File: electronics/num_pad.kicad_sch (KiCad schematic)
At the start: 22 parts, among them J17 Conn_01x04, J18 Conn_01x04, J19 Conn_01x04, J20 Conn_01x04, SW69 SW_SPST, SW70 SW_SPST, SW71 SW_SPST, SW72 SW_SPST, SW73 SW_SPST, SW74 SW_SPST, SW75 SW_SPST, SW76 SW_SPST, SW77 SW_SPST, SW78 SW_SPST, SW79 SW_SPST, SW80 SW_SPST, SW81 SW_SPST, SW82 SW_SPST, SW83 SW_SPST, SW84 SW_SPST, SW85 SW_SPST, U5 PCA9675PW

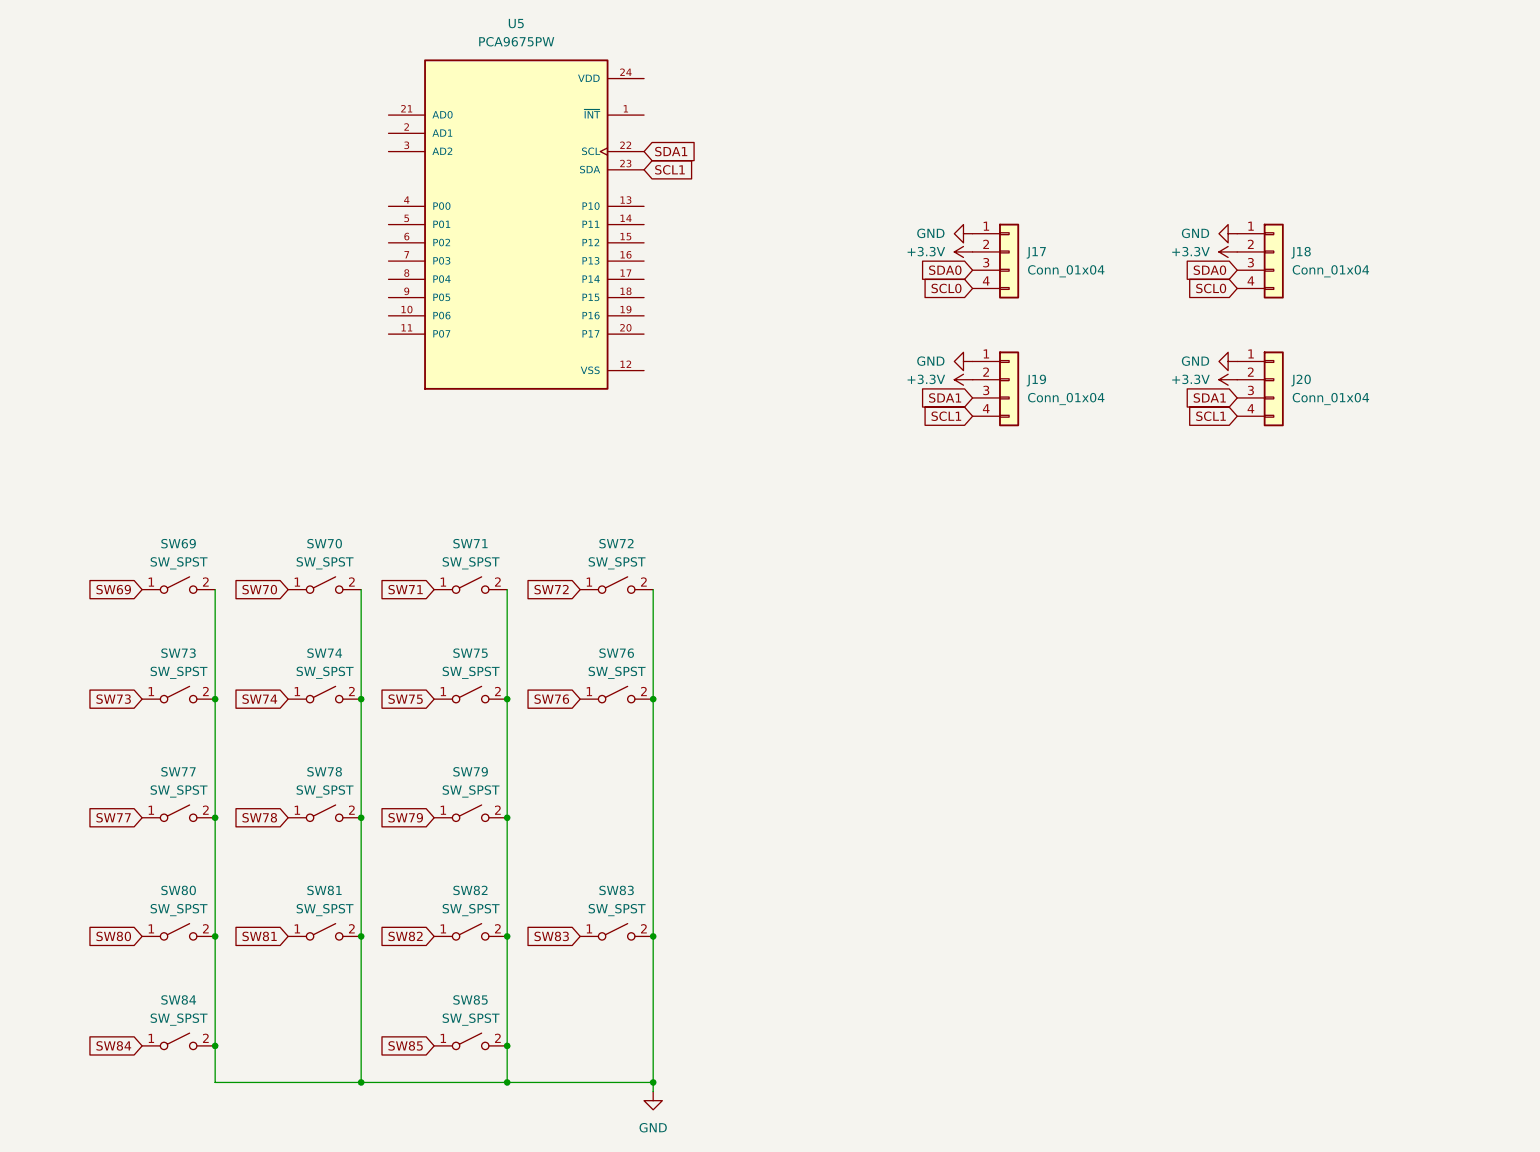
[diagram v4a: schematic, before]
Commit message: begin matrix via diodes
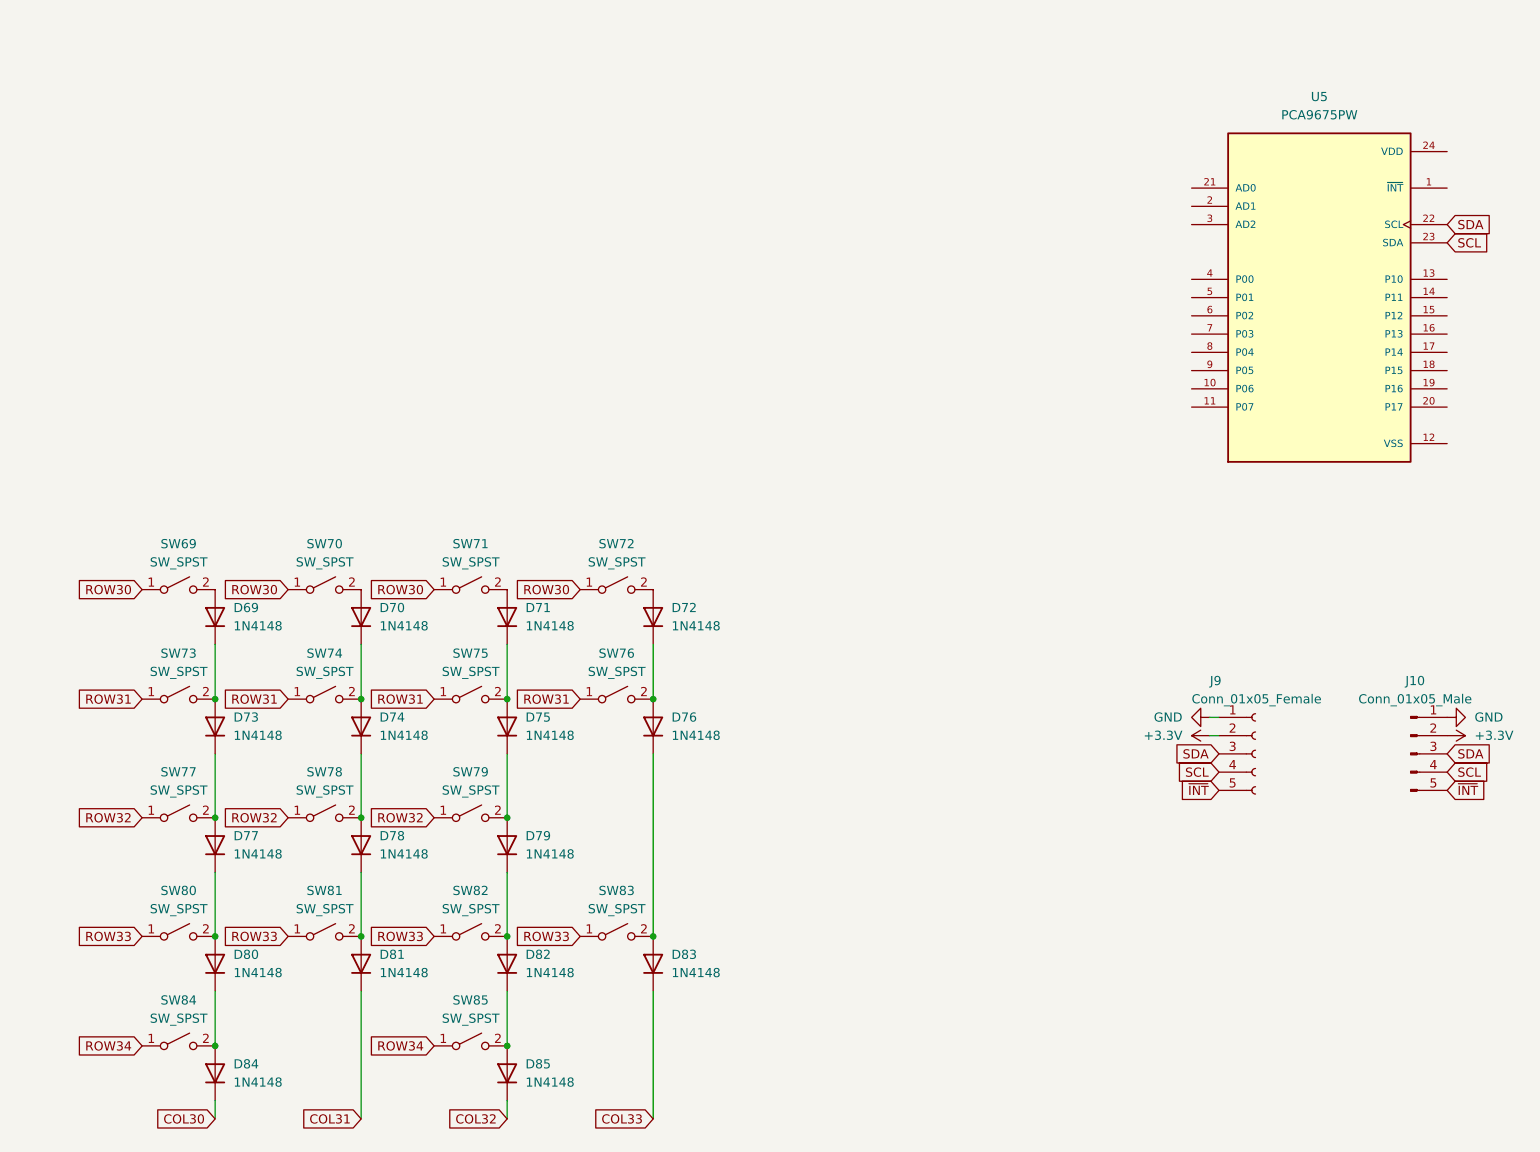
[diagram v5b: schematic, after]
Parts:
- removed J17, J18, J19, J20: Conn_01x04, symbol Connector_Generic:Conn_01x04
- added D69, D70, D71, D72, D73, D74, D75, D76, D77, D78, D79, D80, D81, D82, D83, D84, D85: 1N4148, Diode_SMD:D_SOD-123, symbol Diode:1N4148W
- added J10: Conn_01x05_Male, Connector_PinHeader_2.54mm:PinHeader_1x05_P2.54mm_Vertical, symbol Connector:Conn_01x05_Male
- added J9: Conn_01x05_Female, Connector_PinHeader_2.54mm:PinHeader_1x05_P2.54mm_Vertical, symbol Connector:Conn_01x05_Female
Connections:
- net SW70 is gone; now on net ROW30: SW70.1 (A)
- net SW71 is gone; now on net ROW30: SW71.1 (A)
- net SW72 is gone; now on net ROW30: SW72.1 (A)
- net SW74 is gone; now on net ROW31: SW74.1 (A)
- net SW75 is gone; now on net ROW31: SW75.1 (A)
- net SW76 is gone; now on net ROW31: SW76.1 (A)
- net SW78 is gone; now on net ROW32: SW78.1 (A)
- net SW79 is gone; now on net ROW32: SW79.1 (A)
- net SW81 is gone; now on net ROW33: SW81.1 (A)
- net SW82 is gone; now on net ROW33: SW82.1 (A)
- net SW83 is gone; now on net ROW33: SW83.1 (A)
- net SW85 is gone; now on net ROW34: SW85.1 (A)
- net +3V3: now also J10.2 (Pin_2), J9.2 (Pin_2)
- net GND: now also J10.1 (Pin_1), J9.1 (Pin_1); no longer SW69.2 (B), SW70.2 (B), SW71.2 (B), SW72.2 (B), SW73.2 (B), SW74.2 (B), SW75.2 (B), SW76.2 (B), SW77.2 (B), SW78.2 (B), SW79.2 (B), SW80.2 (B), SW81.2 (B), SW82.2 (B), SW83.2 (B), SW84.2 (B), SW85.2 (B)
- net SCL1 renamed SCL
- net SCL: now also J10.4 (Pin_4), J9.4 (Pin_4)
- net SDA1 renamed SDA
- net SDA: now also J10.3 (Pin_3), J9.3 (Pin_3)
- net SW69 renamed ROW30
- net SW73 renamed ROW31
- net SW77 renamed ROW32
- net SW80 renamed ROW33
- net SW84 renamed ROW34
- new net: D70.1 (K), D74.2 (A), SW74.2 (B)
- new net: D70.2 (A), SW70.2 (B)
- new net: D76.1 (K), D83.2 (A), SW83.2 (B)
- new net: D80.1 (K), D84.2 (A), SW84.2 (B)
- new net: D77.1 (K), D80.2 (A), SW80.2 (B)
- new net: D72.2 (A), SW72.2 (B)
- new net: D69.2 (A), SW69.2 (B)
- new net: D73.1 (K), D77.2 (A), SW77.2 (B)
- new net: D78.1 (K), D81.2 (A), SW81.2 (B)
- new net: D74.1 (K), D78.2 (A), SW78.2 (B)
- new net: D72.1 (K), D76.2 (A), SW76.2 (B)
- new net: D75.1 (K), D79.2 (A), SW79.2 (B)
- new net: D82.1 (K), D85.2 (A), SW85.2 (B)
- new net: D71.1 (K), D75.2 (A), SW75.2 (B)
- new net: D71.2 (A), SW71.2 (B)
- new net: D79.1 (K), D82.2 (A), SW82.2 (B)
- new net: D69.1 (K), D73.2 (A), SW73.2 (B)
- new net COL30: D84.1 (K)
- new net COL31: D81.1 (K)
- new net COL32: D85.1 (K)
- new net COL33: D83.1 (K)
- new net ~{INT}: J10.5 (Pin_5), J9.5 (Pin_5)
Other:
- moved on the sheet: U5

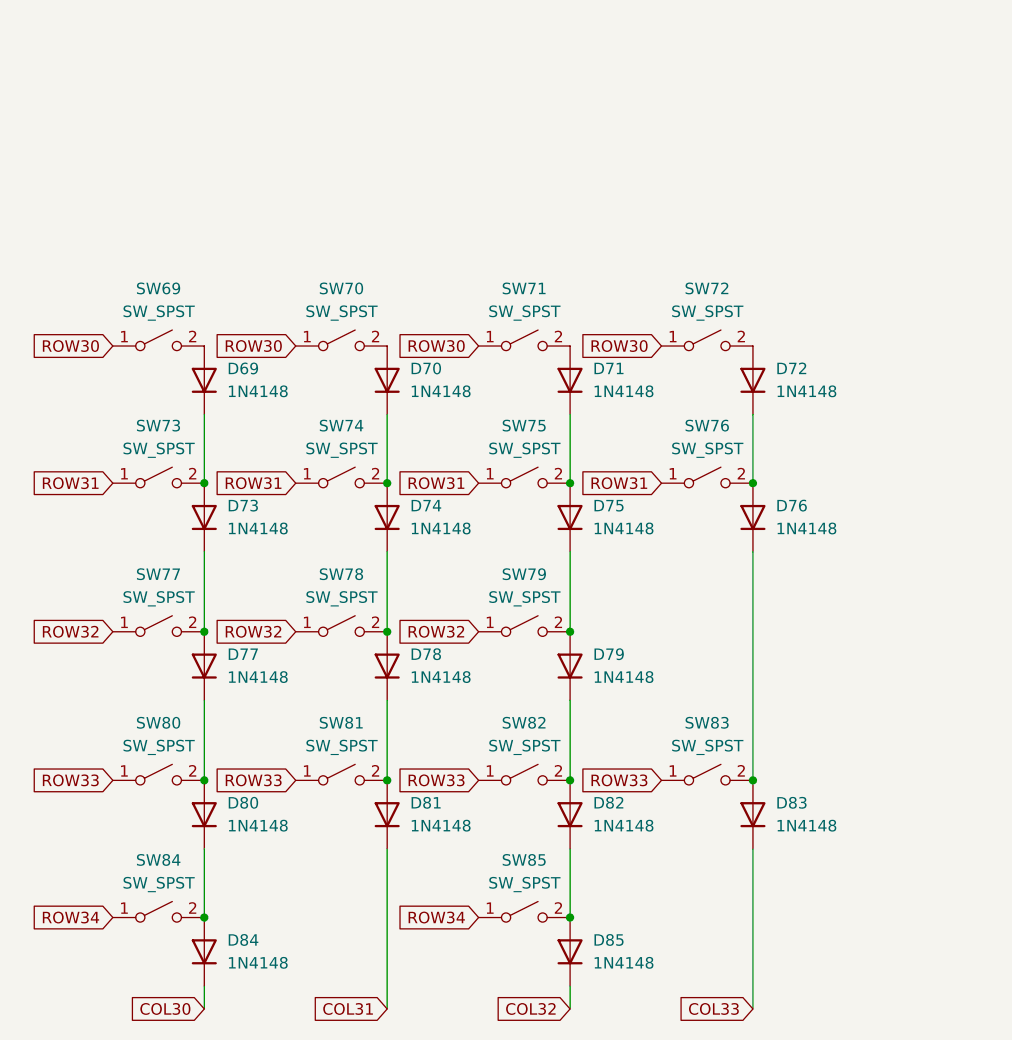
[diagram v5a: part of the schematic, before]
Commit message: fix num pad matrix
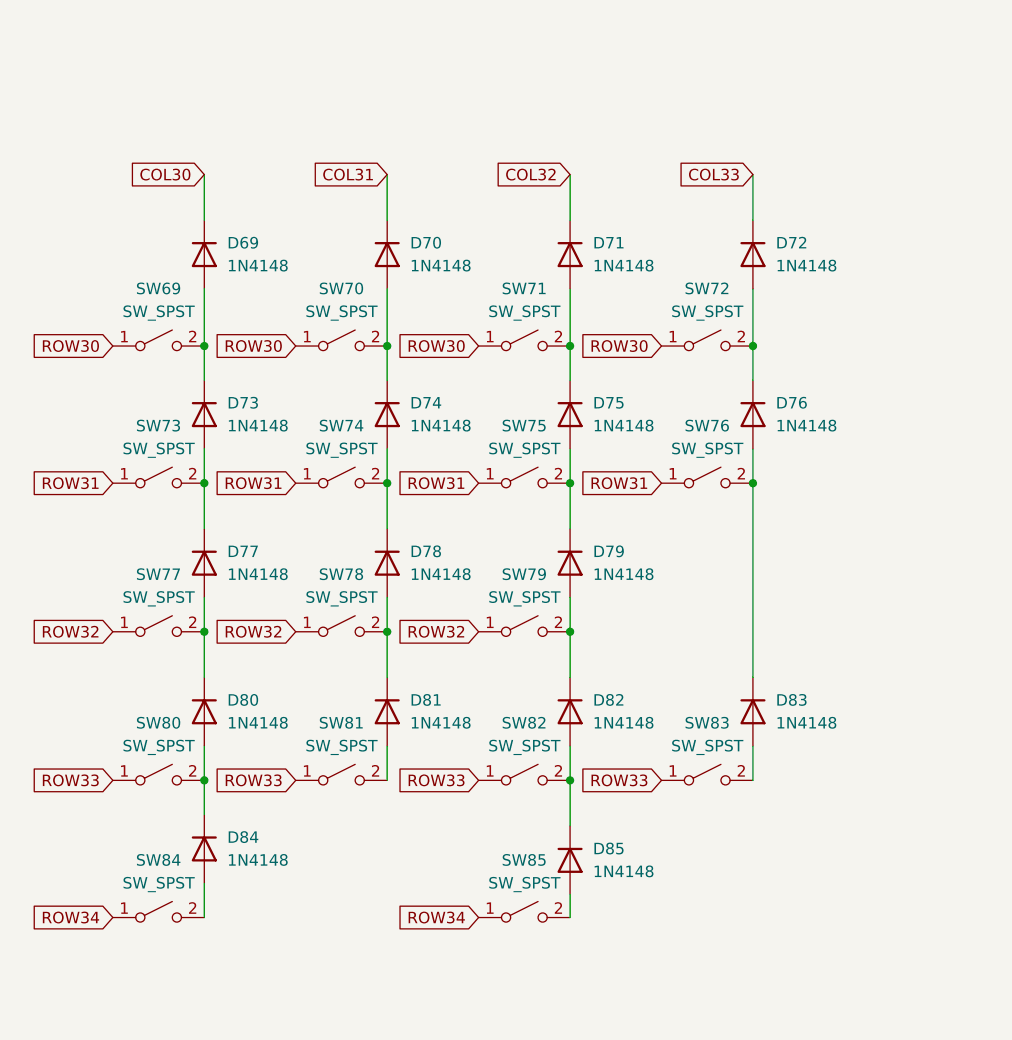
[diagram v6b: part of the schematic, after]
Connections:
- net COL30: now also D69.1 (K); no longer D84.1 (K)
- net COL31: now also D70.1 (K); no longer D81.1 (K)
- net COL32: now also D71.1 (K); no longer D85.1 (K)
- net COL33: now also D72.1 (K); no longer D83.1 (K)
- net at D74.2 (A), SW74.2 (B): now also D78.1 (K); no longer D70.1 (K)
- net at D70.2 (A), SW70.2 (B): now also D74.1 (K)
- net at D83.2 (A), SW83.2 (B): no longer D76.1 (K)
- net at D84.2 (A), SW84.2 (B): no longer D80.1 (K)
- net at D80.2 (A), SW80.2 (B): now also D84.1 (K); no longer D77.1 (K)
- net at D72.2 (A), SW72.2 (B): now also D76.1 (K)
- net at D69.2 (A), SW69.2 (B): now also D73.1 (K)
- net at D77.2 (A), SW77.2 (B): now also D80.1 (K); no longer D73.1 (K)
- net at D81.2 (A), SW81.2 (B): no longer D78.1 (K)
- net at D78.2 (A), SW78.2 (B): now also D81.1 (K); no longer D74.1 (K)
- net at D76.2 (A), SW76.2 (B): now also D83.1 (K); no longer D72.1 (K)
- net at D79.2 (A), SW79.2 (B): now also D82.1 (K); no longer D75.1 (K)
- net at D85.2 (A), SW85.2 (B): no longer D82.1 (K)
- net at D75.2 (A), SW75.2 (B): now also D79.1 (K); no longer D71.1 (K)
- net at D71.2 (A), SW71.2 (B): now also D75.1 (K)
- net at D82.2 (A), SW82.2 (B): now also D85.1 (K); no longer D79.1 (K)
- net at D73.2 (A), SW73.2 (B): now also D77.1 (K); no longer D69.1 (K)
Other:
- moved on the sheet: D69, D70, D71, D72, D73, D74, D75, D76, D77, D78, D79, D80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

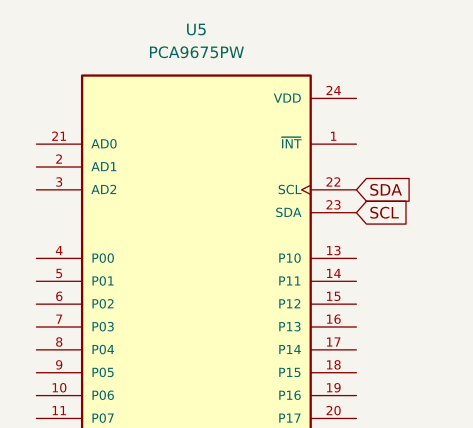
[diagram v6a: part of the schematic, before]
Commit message: fix numpad matrix
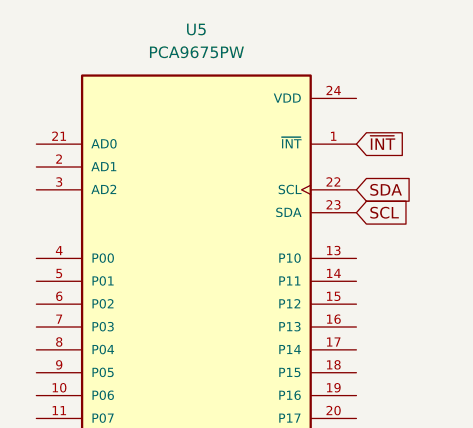
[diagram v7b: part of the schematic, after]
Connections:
- net ~{INT}: now also U5.1 (~{INT})
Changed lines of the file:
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@@
+    )
+  )
+  (global_label "~{INT}" (shape input) (at 237.49 45.72 0) (fields_autoplaced)
+    (effects (font (size 1.27 1.27)) (justify left))
+    (property "Intersheet References" "${INTERSHEET_REFS}" (id 0) (at 242.806 45.7994 0)
+      (effects (font (size 1.27 1.27)) (justify left) hide)
     )
   )

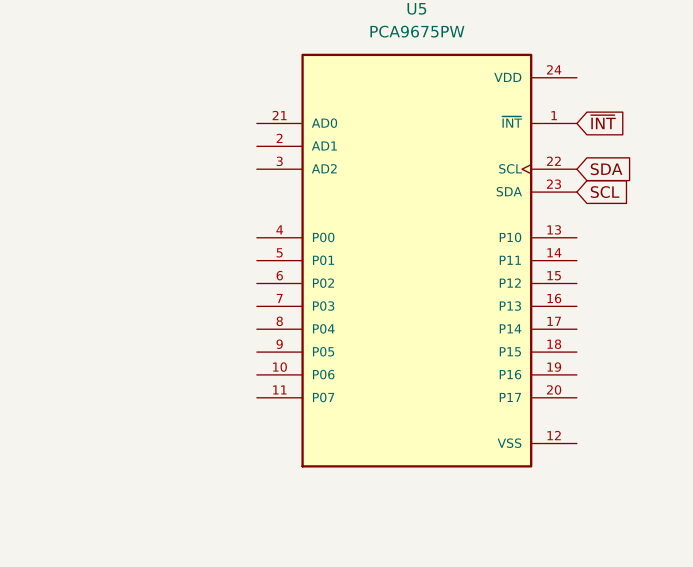
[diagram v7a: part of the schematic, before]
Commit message: connect matrix to io expander
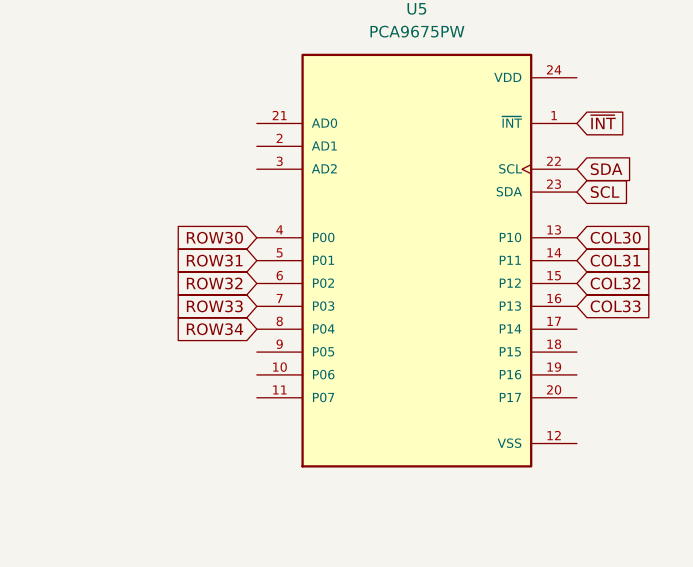
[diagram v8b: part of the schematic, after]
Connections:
- net COL30: now also U5.13 (P10)
- net COL31: now also U5.14 (P11)
- net COL32: now also U5.15 (P12)
- net COL33: now also U5.16 (P13)
- net ROW30: now also U5.4 (P00)
- net ROW31: now also U5.5 (P01)
- net ROW32: now also U5.6 (P02)
- net ROW33: now also U5.7 (P03)
- net ROW34: now also U5.8 (P04)
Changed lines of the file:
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@@
+    )
+  )
+  (global_label "COL32" (shape input) (at 237.49 63.5 0) (fields_autoplaced)
+    (effects (font (size 1.27 1.27)) (justify left))
+    (property "Intersheet References" "${INTERSHEET_REFS}" (id 0) (at 245.9507 63.5794 0)
+      (effects (font (size 1.27 1.27)) (justify left) hide)
     )
   )
@@
     )
   )
+  (global_label "COL31" (shape input) (at 237.49 60.96 0) (fields_autoplaced)
+    (effects (font (size 1.27 1.27)) (justify left))
+    (property "Intersheet References" "${INTERSHEET_REFS}" (id 0) (at 245.9507 61.0394 0)
+      (effects (font (size 1.27 1.27)) (justify left) hide)
+    )
+  )
   (global_label "COL33" (shape input) (at 127 82.55 180) (fields_autoplaced)
     (effects (font (size 1.27 1.27)) (justify right))
@@
     )
   )
+  (global_label "COL30" (shape input) (at 237.49 58.42 0) (fields_autoplaced)
+    (effects (font (size 1.27 1.27)) (justify left))
+    (property "Intersheet References" "${INTERSHEET_REFS}" (id 0) (at 245.9507 58.4994 0)
+      (effects (font (size 1.27 1.27)) (justify left) hide)
+    )
+  )
   (global_label "~{INT}" (shape input) (at 237.49 45.72 0) (fields_autoplaced)
     (effects (font (size 1.27 1.27)) (justify left))
@@
     (effects (font (size 1.27 1.27)) (justify right))
     (property "Intersheet References" "${INTERSHEET_REFS}" (id 0) (at 67.3159 101.5206 0)
+      (effects (font (size 1.27 1.27)) (justify right) hide)
+    )
+  )
+  (global_label "ROW31" (shape input) (at 201.93 60.96 180) (fields_autoplaced)
+    (effects (font (size 1.27 1.27)) (justify right))
+    (property "Intersheet References" "${INTERSHEET_REFS}" (id 0) (at 193.0459 60.8806 0)
       (effects (font (size 1.27 1.27)) (justify right) hide)
     )
@@
     )
   )
+  (global_label "ROW32" (shape input) (at 201.93 63.5 180) (fields_autoplaced)
+    (effects (font (size 1.27 1.27)) (justify right))
+    (property "Intersheet References" "${INTERSHEET_REFS}" (id 0) (at 193.0459 63.4206 0)
+      (effects (font (size 1.27 1.27)) (justify right) hide)
+    )
+  )
   (global_label "ROW33" (shape input) (at 96.52 149.86 180) (fields_autoplaced)
     (effects (font (size 1.27 1.27)) (justify right))
@@
     )
   )
+  (global_label "COL33" (shape input) (at 237.49 66.04 0) (fields_autoplaced)
+    (effects (font (size 1.27 1.27)) (justify left))
+    (property "Intersheet References" "${INTERSHEET_REFS}" (id 0) (at 245.9507 66.1194 0)
+      (effects (font (size 1.27 1.27)) (justify left) hide)
+    )
+  )
   (global_label "ROW33" (shape input) (at 76.2 149.86 180) (fields_autoplaced)
     (effects (font (size 1.27 1.27)) (justify right))
@@
     (property "Intersheet References" "${INTERSHEET_REFS}" (id 0) (at 243.4107 126.9206 0)
       (effects (font (size 1.27 1.27)) (justify left) hide)
+    )
+  )
+  (global_label "ROW33" (shape input) (at 201.93 66.04 180) (fields_autoplaced)
+    (effects (font (size 1.27 1.27)) (justify right))
+    (property "Intersheet References" "${INTERSHEET_REFS}" (id 0) (at 193.0459 65.9606 0)
+      (effects (font (size 1.27 1.27)) (justify right) hide)
+    )
+  )
+  (global_label "ROW34" (shape input) (at 201.93 68.58 180) (fields_autoplaced)
+    (effects (font (size 1.27 1.27)) (justify right))
+    (property "Intersheet References" "${INTERSHEET_REFS}" (id 0) (at 193.0459 68.5006 0)
+      (effects (font (size 1.27 1.27)) (justify right) hide)
     )
   )
@@
       (effects (font (size 1.27 1.27)) (justify right) hide)
     )
+  )
+  (global_label "ROW30" (shape input) (at 201.93 58.42 180) (fields_autoplaced)
+    (effects (font (size 1.27 1.27)) (justify right))
+    (property "Intersheet References" "${INTERSHEET_REFS}" (id 0) (at 193.0459 58.3406 0)
+      (effects (font (size 1.27 1.27)) (justify right) hide)
+    )
